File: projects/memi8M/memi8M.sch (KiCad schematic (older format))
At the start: 0 parts

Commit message: 1. memi8M project update. 2. New mods added.
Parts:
- added C? (x2): C, symbol C
- added J?: Conn_01x06, symbol Conn_01x06
- added J?: Conn_01x02, symbol Conn_01x02
- added J?: Conn_01x03, symbol Conn_01x03
- added JP?: DUAL_JUMPER, symbol DUAL_JUMPER
- added JP? (x3): SINGLE_JUMPER, symbol SINGLE_JUMPER
- added R? (x3): R, symbol R
- added U? (x4): 74HC595N, symbol 74HC595N
- added U? (x3): 74LVC245, 74LVC245_SO20, symbol 74LVC245
- added U?: SFC_MaskRom_32pin, symbol SFC_MaskRom_32pin
- added U?: SST39VF1681_1682, symbol SST39VF1681_1682
- added U?: 74LVC4245, symbol 74LVC4245
- added U?: 74LS166N, symbol 74LS166N
- added U?: LD1117S33TR_SOT223, TO_SOT_Packages_SMD:SOT-223-3Lead_TabPin2, symbol LD1117S33TR_SOT223
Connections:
- new net: U?.14 (SER), U?.9 (~QH) (x3)
- new net: JP?.2 (B), U?.2 (DIR)
- new net: JP?.2 (B), R?.2 (x3)
- new net +3V3: C?.1, U?.1 (DIR), U?.1 (DIR), U?.1 (DIR), U?.12 (RST), U?.14 (WP), U?.2 (VO), U?.20 (VCC), U?.20 (VCC), U?.20 (VCC), U?.23 (VCCB), U?.24 (VCCB), U?.37 (VDD)
- new net A0_3V: U?.18 (B1), U?.45 (A0)
- new net A0_5V: U?.12 (A0), U?.15 (QA), U?.2 (A1)
- new net A10_3V: U?.16 (B3), U?.7 (A10)
- new net A10_5V: U?.2 (QC), U?.23 (A10), U?.4 (A3)
- new net A11_3V: U?.15 (B4), U?.6 (A11)
- new net A11_5V: U?.25 (A11), U?.3 (QD), U?.5 (A4)
- new net A12_3V: U?.14 (B5), U?.5 (A12)
- new net A12_5V: U?.4 (A12), U?.4 (QE), U?.6 (A5)
- new net A13_3V: U?.13 (B6), U?.4 (A13)
- new net A13_5V: U?.28 (A13), U?.5 (QF), U?.7 (A6)
- new net A14_3V: U?.12 (B7), U?.3 (A14)
- new net A14_5V: U?.29 (A14), U?.6 (QG), U?.8 (A7)
- new net A15_3V: U?.11 (B8), U?.2 (A15)
- new net A15_5V: U?.3 (A15), U?.7 (QH), U?.9 (A8)
- new net A16_3V: U?.1 (A16), U?.18 (B1)
- new net A16_5V: U?.15 (QA), U?.2 (A1), U?.24 (A16)
- new net A17_3V: U?.17 (B2), U?.48 (A17)
- new net A17_5V: U?.1 (A17), U?.1 (QB), U?.3 (A2)
- new net A18_3V: U?.16 (B3), U?.17 (A18)
- new net A18_5V: U?.2 (A18), U?.2 (QC), U?.4 (A3)
- new net A19_3V: U?.15 (B4), U?.16 (A19)
- new net A19_5V: U?.3 (QD), U?.30 (A19), U?.5 (A4)
- new net A1_3V: U?.17 (B2), U?.25 (A1)
- new net A1_5V: U?.1 (QB), U?.11 (A1), U?.3 (A2)
- new net A2_3V: U?.16 (B3), U?.24 (A2)
- new net A2_5V: U?.10 (A2), U?.2 (QC), U?.4 (A3)
- new net A3_3V: U?.15 (B4), U?.23 (A3)
- new net A3_5V: U?.3 (QD), U?.5 (A4), U?.9 (A3)
- new net A4_3V: U?.14 (B5), U?.22 (A4)
- new net A4_5V: U?.4 (QE), U?.6 (A5), U?.8 (A4)
- new net A5_3V: U?.13 (B6), U?.21 (A5)
- new net A5_5V: U?.5 (QF), U?.7 (A5), U?.7 (A6)
- new net A6_3V: U?.12 (B7), U?.20 (A6)
- new net A6_5V: U?.6 (A6), U?.6 (QG), U?.8 (A7)
- new net A7_3V: U?.11 (B8), U?.19 (A7)
- new net A7_5V: U?.5 (A7), U?.7 (QH), U?.9 (A8)
- new net A8_3V: U?.18 (A8), U?.18 (B1)
- new net A8_5V: U?.15 (QA), U?.2 (A1), U?.27 (A8)
- new net A9_3V: U?.17 (B2), U?.8 (A9)
- new net A9_5V: U?.1 (QB), U?.26 (A9), U?.3 (A2)
- new net D0_3V: U?.21 (B1), U?.29 (DQ0)
- new net D0_5V: U?.13 (Q0), U?.15 (QA), U?.2 (A), U?.3 (A1)
- new net D1_3V: U?.20 (B2), U?.31 (DQ1)
- new net D1_5V: U?.1 (QB), U?.14 (Q1), U?.3 (B), U?.4 (A2)
- new net D2_3V: U?.19 (B3), U?.33 (DQ2)
- new net D2_5V: U?.15 (Q2), U?.2 (QC), U?.4 (C), U?.5 (A3)
- new net D3_3V: U?.18 (B4), U?.35 (DQ3)
- new net D3_5V: U?.17 (Q3), U?.3 (QD), U?.5 (D), U?.6 (A4)
- new net D4_3V: U?.17 (B5), U?.38 (DQ4)
- new net D4_5V: U?.10 (E), U?.18 (Q4), U?.4 (QE), U?.7 (A5)
- new net D5_3V: U?.16 (B6), U?.40 (DQ5)
- new net D5_5V: U?.11 (F), U?.19 (Q5), U?.5 (QF), U?.8 (A6)
- new net D6_3V: U?.15 (B7), U?.42 (DQ6)
- new net D6_5V: U?.12 (G), U?.20 (Q6), U?.6 (QG), U?.9 (A7)
- new net D7_3V: U?.14 (B8), U?.44 (DQ7)
- new net D7_5V: U?.10 (A8), U?.14 (H), U?.21 (Q7), U?.7 (QH)
- new net FLASH_CE: U?.13 (B6), U?.26 (CE)
- new net FLASH_OE: U?.12 (B7), U?.28 (OE)
- new net GND: C?.2, C?.2, J?.2 (Pin_2), JP?.3 (C), R?.1, U?.1 (Ds), U?.1 (GND), U?.10 (GND), U?.10 (GND), U?.10 (GND), U?.11 (GND), U?.12 (GND), U?.13 (GND), U?.16 (VSS), U?.19 (OE), U?.19 (OE), U?.19 (OE), U?.27 (VSS), U?.46 (VSS), U?.8 (GND), U?.8 (GND), U?.8 (GND), U?.8 (GND), U?.8 (GND)
- new net ROM_CE: J?.1 (Pin_1), U?.22 (CE), U?.7 (A6)
- new net ROM_OE: J?.2 (Pin_2), U?.31 (OE), U?.8 (A7)
- new net SI_OE_A: J?.5 (Pin_5), JP?.1 (A), U?.13 (G), U?.13 (G), U?.13 (G)
- new net SI_OE_D: J?.6 (Pin_6), JP?.1 (A), U?.13 (G)
- new net SI_RCLK: J?.4 (Pin_4), U?.12 (RCLK), U?.12 (RCLK), U?.12 (RCLK), U?.12 (RCLK)
- new net SI_SER: J?.1 (Pin_1), U?.14 (SER)
- new net SI_SRCLK: J?.2 (Pin_2), U?.11 (SRCLK), U?.11 (SRCLK), U?.11 (SRCLK), U?.11 (SRCLK)
- new net SI_SRCLR: J?.3 (Pin_3), U?.10 (SRCLR), U?.10 (SRCLR), U?.10 (SRCLR), U?.10 (SRCLR)
- new net SO_CLK: U?.7 (Clk)
- new net SO_CLK_INH: U?.6 (CE)
- new net SO_CLR: JP?.1 (A), U?.9 (Clr)
- new net SO_SHLD: U?.15 (PE)
- new net VCC: C?.1, J?.1 (Pin_1), R?.1, R?.1, U?.1 (VCCA), U?.16 (VCC), U?.16 (VCC), U?.16 (VCC), U?.16 (VCC), U?.16 (VCC), U?.3 (VI), U?.32 (VCC)
- new net WE_3V: U?.11 (WE), U?.14 (B5)
- new net WE_5V: J?.3 (Pin_3), U?.6 (A5)
- no-connect marks 0 -> 6
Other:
- note added: "Jumpers (or DIPs)"

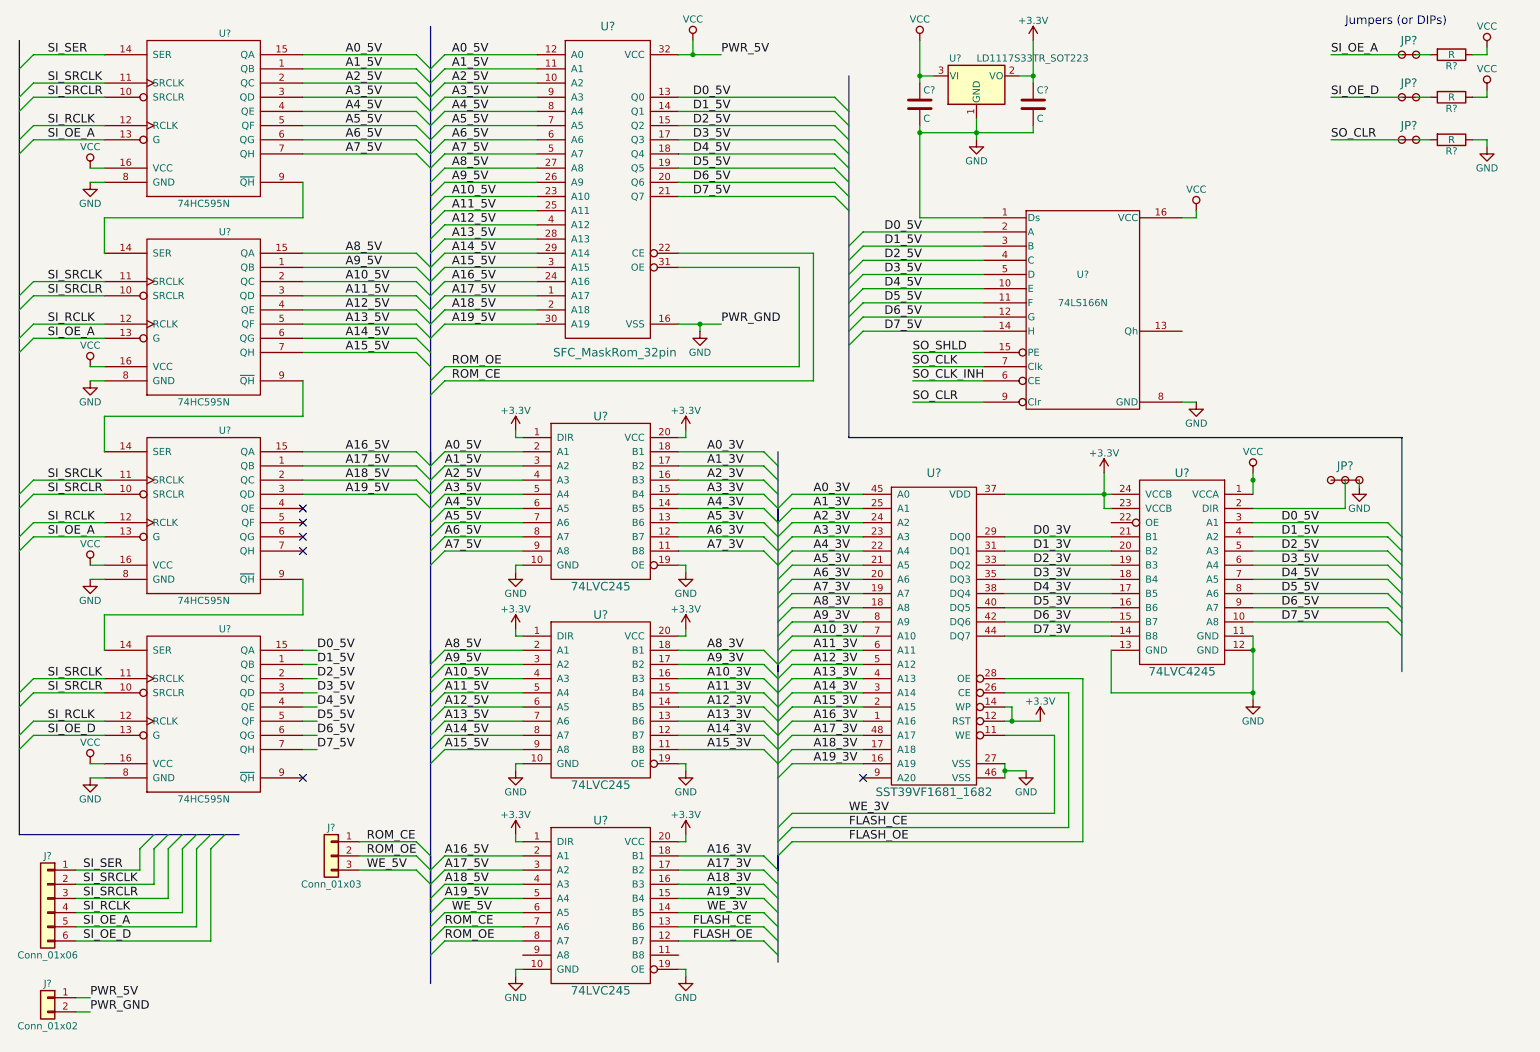
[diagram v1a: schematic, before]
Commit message: 1. Sch of memi8M completed. 2. New lib elements and improvements. 3. BOM generated.
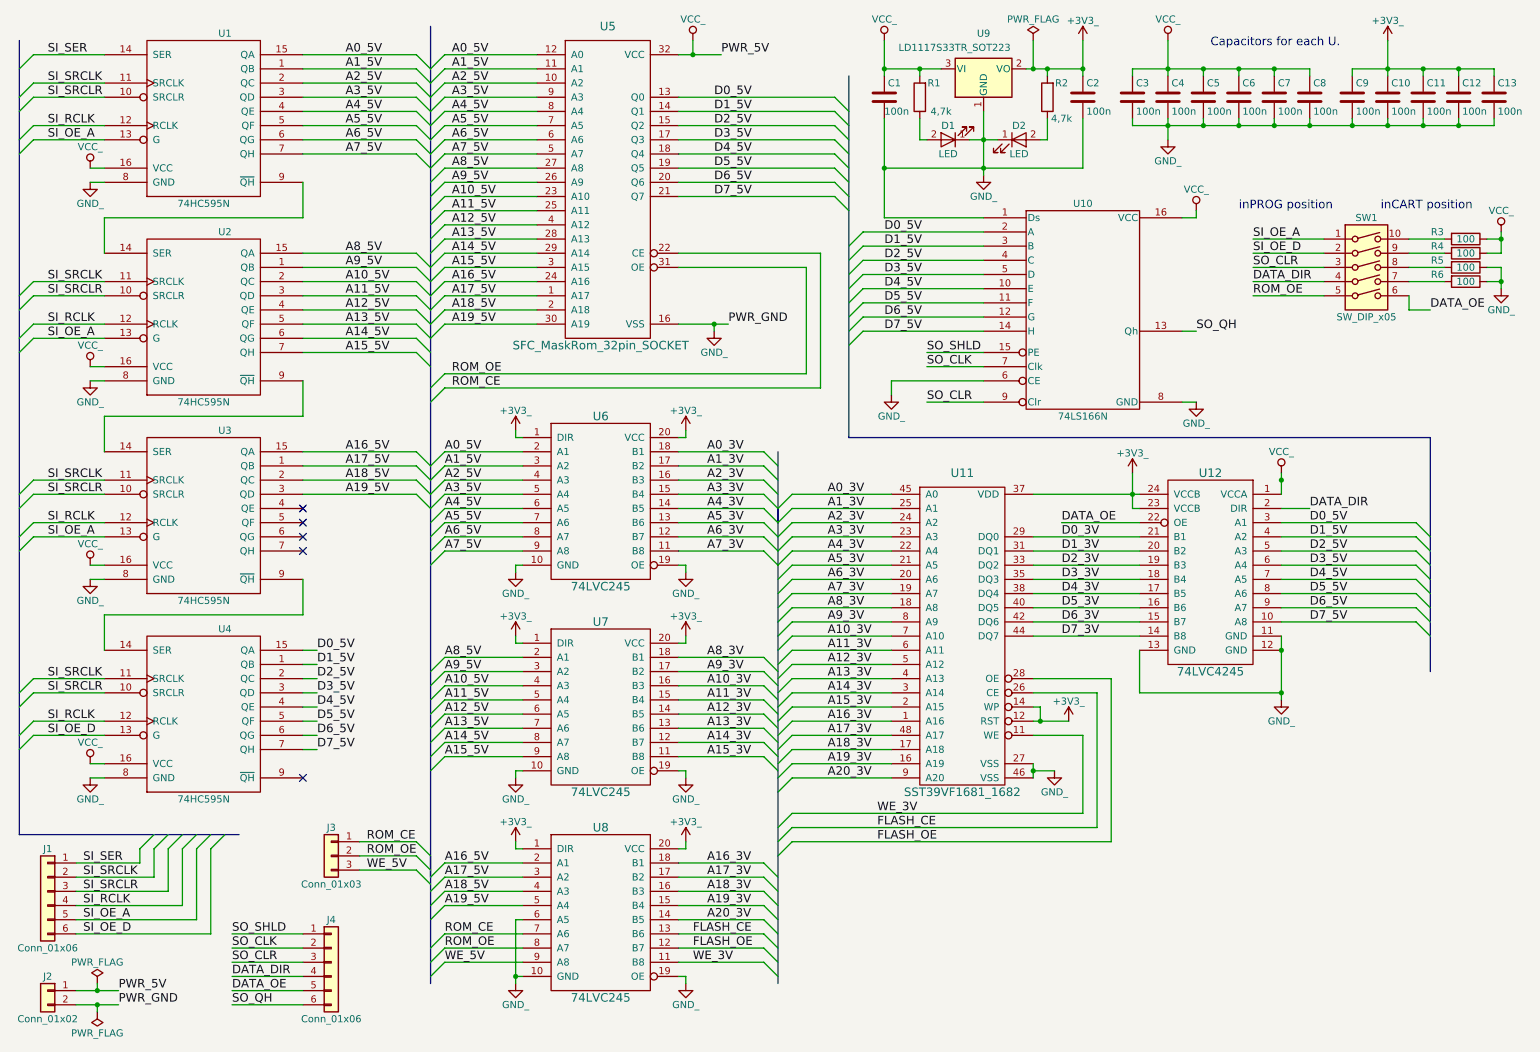
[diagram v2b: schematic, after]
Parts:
- removed JP?: DUAL_JUMPER, symbol DUAL_JUMPER
- removed JP? (x3): SINGLE_JUMPER, symbol SINGLE_JUMPER
- added C10, C11, C12, C13, C3, C4, C5, C6, C7, C8, C9: 100n, symbol C
- added D1, D2: LED, symbol LED
- added J4: Conn_01x06, symbol Conn_01x06
- added R1, R2: 4,7k, symbol R
- added R6: 100, symbol R
- added SW1: SW_DIP_x05, symbol SW_DIP_x05
- C1, C2: renamed from C?; value C -> 100n
- R3, R4, R5: renamed from R?; value R -> 100
- U5: renamed from U?; value SFC_MaskRom_32pin -> SFC_MaskRom_32pin_SOCKET
- gave numbers to parts that had none: 14
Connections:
- net SO_CLK_INH is gone; now on net GND_: U10.6 (CE)
- net ROM_OE: now also SW1.5
- net SI_OE_A: now also SW1.1
- net SI_OE_D: now also SW1.2
- net SO_CLK: now also J4.2 (Pin_2)
- net SO_CLR: now also J4.3 (Pin_3), SW1.3
- net SO_SHLD: now also J4.1 (Pin_1)
- net WE_3V: now also U8.11 (B8); no longer U8.14 (B5)
- net WE_5V: now also U8.9 (A8); no longer U8.6 (A5)
- net A20_3V: now reaches U11.9 (A20)
- net A20_3V: now also U8.14 (B5)
- net DATA_DIR: now reaches U12.2 (DIR)
- net DATA_DIR: now also J4.4 (Pin_4), SW1.4
- net DATA_OE: now reaches U12.22 (OE)
- net DATA_OE: now also J4.5 (Pin_5), SW1.6
- net SO_QH: now reaches U10.13 (Qh)
- net SO_QH: now also J4.6 (Pin_6)
- net at R3.2: now also SW1.10
- net at R5.2: now also SW1.8
- net at R4.2: now also SW1.9
- net +3V3 renamed +3V3_
- net +3V3_: now also C10.1, C11.1, C12.1, C13.1, C9.1, R2.2
- net GND renamed GND_
- net GND_: now also U8.6 (A5), C10.2, C11.2, C12.2, C13.2, C3.2, C4.2, C5.2, C6.2, C7.2, C8.2, C9.2, D1.1 (K), D2.1 (K), R6.1
- net VCC renamed VCC_
- net VCC_: now also C3.1, C4.1, C5.1, C6.1, C7.1, C8.1, R1.2
- new net: R6.2, SW1.7
- new net: D1.2 (A), R1.1
- new net: D2.2 (A), R2.1
- no-connect marks 6 -> 5
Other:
- note added: "Capacitors for each U."
- note added: "inCART position"
- note added: "inPROG position"
- note removed: "Jumpers (or DIPs)"
- moved on the sheet: C1, C2, J1, J2, R3, R4, R5, U11, U12, U7, U8, U9

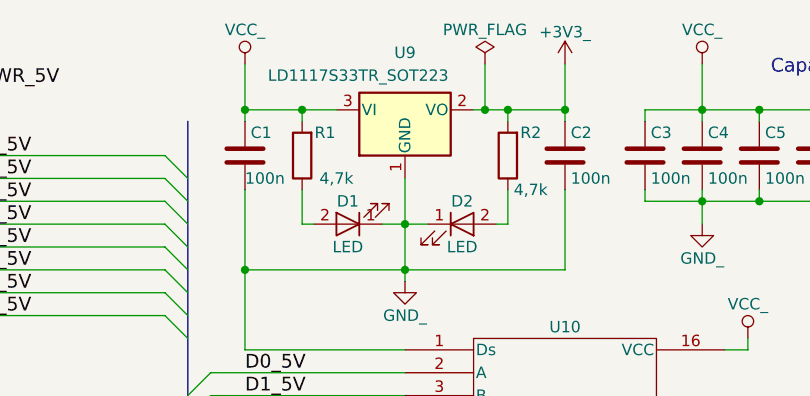
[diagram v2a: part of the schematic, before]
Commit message: Added PDIP32 package and PINHEAD1x16. Added keywords to all packages. Added LDO 3.3V to lib, with 4 pins (4th is the surface to match package).
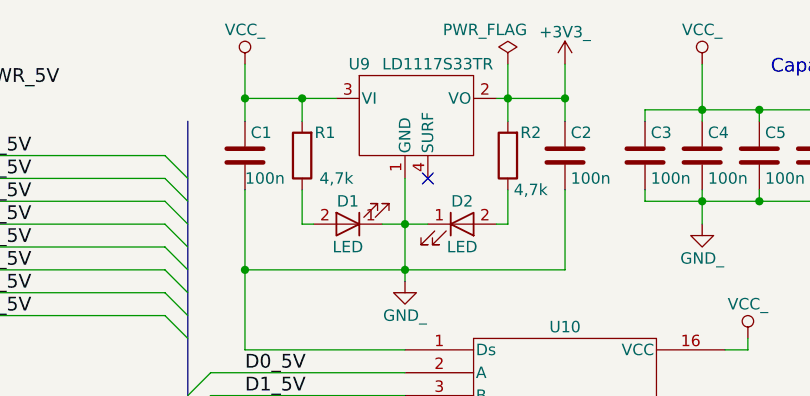
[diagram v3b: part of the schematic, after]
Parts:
- removed U9: LD1117S33TR_SOT223, TO_SOT_Packages_SMD:SOT-223-3Lead_TabPin2, symbol LD1117S33TR_SOT223
- added U9: LD1117S33TR, symbol LD1117S33TR
- J1, J4: footprint (none) -> PINHEAD1x6
- J2: footprint (none) -> PINHEAD1x2
- J3: footprint (none) -> PINHEAD1x3
- U1, U2, U3, U4: footprint (none) -> SO16
- U5: footprint (none) -> PDIP32
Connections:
- net +3V3_: now also U9.2 (VO)
- net GND_: now also U9.1 (GND)
- net VCC_: now also U9.3 (VI)
- no-connect marks 5 -> 6
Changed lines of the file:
@@
 F 0 "U1" H 2050 1900 50  0000 C CNN
 F 1 "74HC595N" H 1900 700 50  0000 C CNN
-F 2 "" H 1900 1300 50  0001 C CNN
+F 2 "SO16" H 1900 1300 50  0001 C CNN
 F 3 "" H 1900 1300 50  0001 C CNN
 	1    1900 1300
@@
 F 0 "U2" H 2050 3300 50  0000 C CNN
 F 1 "74HC595N" H 1900 2100 50  0000 C CNN
-F 2 "" H 1900 2700 50  0001 C CNN
+F 2 "SO16" H 1900 2700 50  0001 C CNN
 F 3 "" H 1900 2700 50  0001 C CNN
 	1    1900 2700
@@
 F 0 "U3" H 2050 4700 50  0000 C CNN
 F 1 "74HC595N" H 1900 3500 50  0000 C CNN
-F 2 "" H 1900 4100 50  0001 C CNN
+F 2 "SO16" H 1900 4100 50  0001 C CNN
 F 3 "" H 1900 4100 50  0001 C CNN
 	1    1900 4100
@@
 F 0 "U5" H 4750 2450 60  0000 C CNN
 F 1 "SFC_MaskRom_32pin_SOCKET" H 4700 200 60  0000 C CNN
-F 2 "" H 4750 2450 60  0001 C CNN
+F 2 "PDIP32" H 4750 2450 60  0001 C CNN
 F 3 "" H 4750 2450 60  0001 C CNN
 	1    4750 1550
@@
 F 0 "U4" H 2050 6100 50  0000 C CNN
 F 1 "74HC595N" H 1900 4900 50  0000 C CNN
-F 2 "" H 1900 5500 50  0001 C CNN
+F 2 "SO16" H 1900 5500 50  0001 C CNN
 F 3 "" H 1900 5500 50  0001 C CNN
 	1    1900 5500
@@
 $EndComp
 $Comp
-L LD1117S33TR_SOT223 U9
-U 1 1 5C482D93
-P 7400 950
-F 0 "U9" H 7400 1200 50  0000 C CNN
-F 1 "LD1117S33TR_SOT223" H 6800 1100 50  0000 L CNN
-F 2 "TO_SOT_Packages_SMD:SOT-223-3Lead_TabPin2" H 7400 1150 50  0001 C CNN
-F 3 "" H 7500 700 50  0001 C CNN
-	1    7400 950
-	1    0    0    -1
-$EndComp
-$Comp
 L C C1
 U 1 1 5C483724
@@
 F 0 "J1" H 800 7050 50  0000 C CNN
 F 1 "Conn_01x06" H 800 6350 50  0000 C CNN
-F 2 "" H 800 6750 50  0001 C CNN
+F 2 "PINHEAD1x6" H 800 6750 50  0001 C CNN
 F 3 "" H 800 6750 50  0001 C CNN
 	1    800  6750
@@
 F 0 "J2" H 800 7550 50  0000 C CNN
 F 1 "Conn_01x02" H 800 7250 50  0000 C CNN
-F 2 "" H 800 7450 50  0001 C CNN
+F 2 "PINHEAD1x2" H 800 7450 50  0001 C CNN
 F 3 "" H 800 7450 50  0001 C CNN
 	1    800  7450
@@
 F 0 "J3" H 2800 6700 50  0000 C CNN
 F 1 "Conn_01x03" H 2800 6300 50  0000 C CNN
-F 2 "" H 2800 6500 50  0001 C CNN
+F 2 "PINHEAD1x3" H 2800 6500 50  0001 C CNN
 F 3 "" H 2800 6500 50  0001 C CNN
 	1    2800 6500
@@
 F 0 "J4" H 2800 7550 50  0000 C CNN
 F 1 "Conn_01x06" H 2800 6850 50  0000 C CNN
-F 2 "" H 2800 7250 50  0001 C CNN
+F 2 "PINHEAD1x6" H 2800 7250 50  0001 C CNN
 F 3 "" H 2800 7250 50  0001 C CNN
 	1    2800 7250
@@
 	6700 750  6700 1000
 Wire Wire Line
-	6700 950  7100 950
-Wire Wire Line
-	7700 950  8100 950
-Wire Wire Line
 	8100 750  8100 1000
-Connection ~ 6700 950
-Connection ~ 8100 950
 Wire Wire Line
 	5250 7350 5300 7350
@@
 	2600 7550 2100 7550
 Wire Wire Line
-	7400 1250 7400 1700
-Wire Wire Line
 	7300 1450 7500 1450
-Connection ~ 7400 1450
 Wire Wire Line
 	8100 1650 8100 1300
@@
 Wire Wire Line
 	6700 1650 8100 1650
-Connection ~ 7400 1650
 Wire Wire Line
 	6950 1300 6950 1450
@@
 Wire Wire Line
 	7850 1450 7850 1300
-Wire Wire Line
-	6950 1000 6950 950
-Connection ~ 6950 950
-Wire Wire Line
-	7850 1000 7850 950
-Connection ~ 7850 950
 Connection ~ 6700 1650
 $Comp
@@
 L PWR_FLAG #FLG041
 U 1 1 5C51F77C
-P 7750 750
-F 0 "#FLG041" H 7750 825 50  0001 C CNN
+P 7850 750
+F 0 "#FLG041" H 7850 825 50  0001 C CNN
 F 1 "PWR_FLAG" H 7750 900 50  0000 C CNN
-F 2 "" H 7750 750 50  0001 C CNN
-F 3 "" H 7750 750 50  0001 C CNN
-	1    7750 750
-	1    0    0    -1
-$EndComp
-Wire Wire Line
-	7750 750  7750 950
-Connection ~ 7750 950
+F 2 "" H 7850 750 50  0001 C CNN
+F 3 "" H 7850 750 50  0001 C CNN
+	1    7850 750
+	1    0    0    -1
+$EndComp
+$Comp
+L LD1117S33TR U9
+U 1 1 5C613B70
+P 7450 950
+F 0 "U9" H 7200 1150 50  0000 C CNN
+F 1 "LD1117S33TR" H 7300 1150 50  0000 L CNN
+F 2 "" H 6600 1150 50  0001 C CNN
+F 3 "" H 6700 750 50  0001 C CNN
+	1    7450 950
+	1    0    0    -1
+$EndComp
+Wire Wire Line
+	6700 900  7100 900
+Wire Wire Line
+	6950 900  6950 1000
+Wire Wire Line
+	7800 900  8100 900
+Wire Wire Line
+	7850 750  7850 1000
+Connection ~ 7850 900
+Connection ~ 8100 900
+Connection ~ 6700 900
+Connection ~ 6950 900
+Wire Wire Line
+	7400 1250 7400 1700
+Connection ~ 7400 1650
+Connection ~ 7400 1450
+NoConn ~ 7500 1250
 $EndSCHEMATC
